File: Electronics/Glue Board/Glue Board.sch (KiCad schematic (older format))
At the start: 0 parts

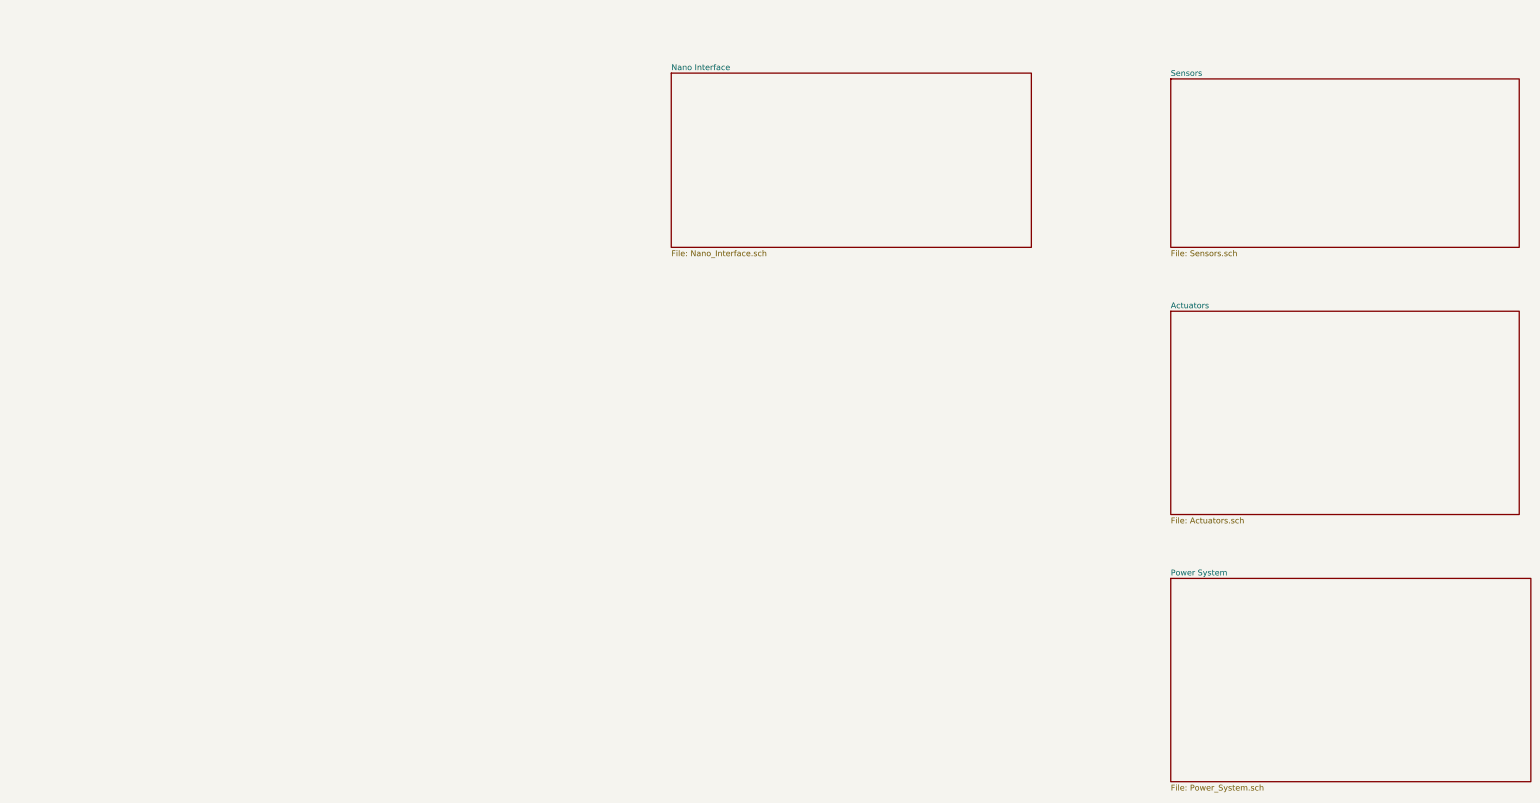
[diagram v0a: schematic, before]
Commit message: Finished the schematic for the most parts
Finished the schematic for the most parts
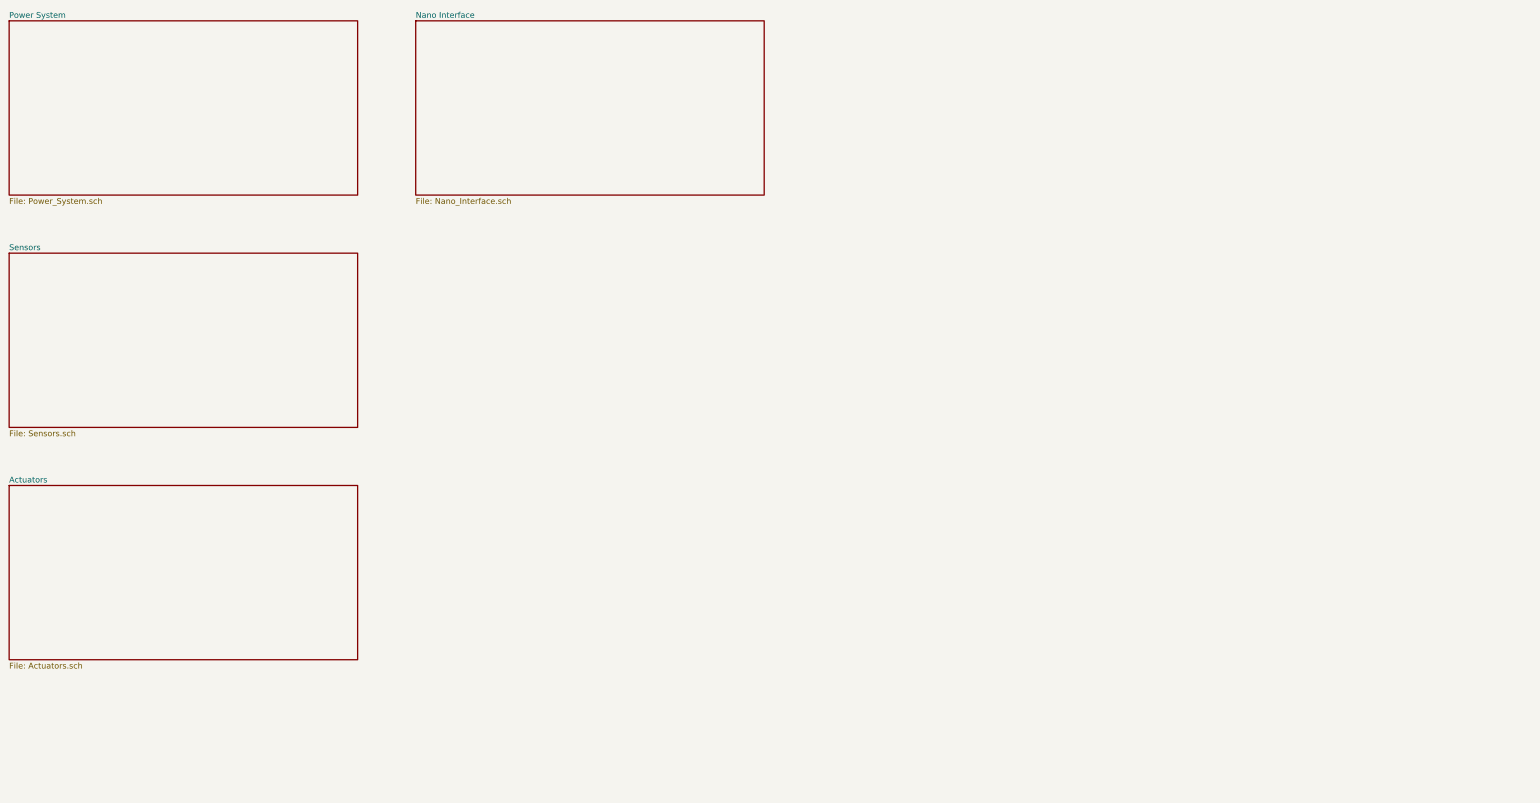
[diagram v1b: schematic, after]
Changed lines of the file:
@@
 $EndDescr
 $Sheet
-S 11000 5800 3100 1750
+S 1000 1000 3000 1500
 U 5E05834F
 F0 "Power System" 50
@@
 $EndSheet
 $Sheet
-S 11000 3500 3000 1750
+S 1000 5000 3000 1500
 U 5E058475
 F0 "Actuators" 50
@@
 $EndSheet
 $Sheet
-S 11000 1500 3000 1450
+S 1000 3000 3000 1500
 U 5E058596
 F0 "Sensors" 50
@@
 $EndSheet
 $Sheet
-S 6700 1450 3100 1500
+S 4500 1000 3000 1500
 U 5E0731B8
 F0 "Nano Interface" 50
